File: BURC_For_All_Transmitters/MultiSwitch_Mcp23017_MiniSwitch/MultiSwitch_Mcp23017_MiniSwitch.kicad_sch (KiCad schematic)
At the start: 27 parts, among them J1 MPC23017_MODULE, J2 I2C_INPUT, J3 I2C_INPUT, J4 I2C_INPUT, J5 I2C_INPUT, J6 PCF8574, J7 PCF8574, J8 PCF8575, SW1 SW_SPST, SW10 SW_SPST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

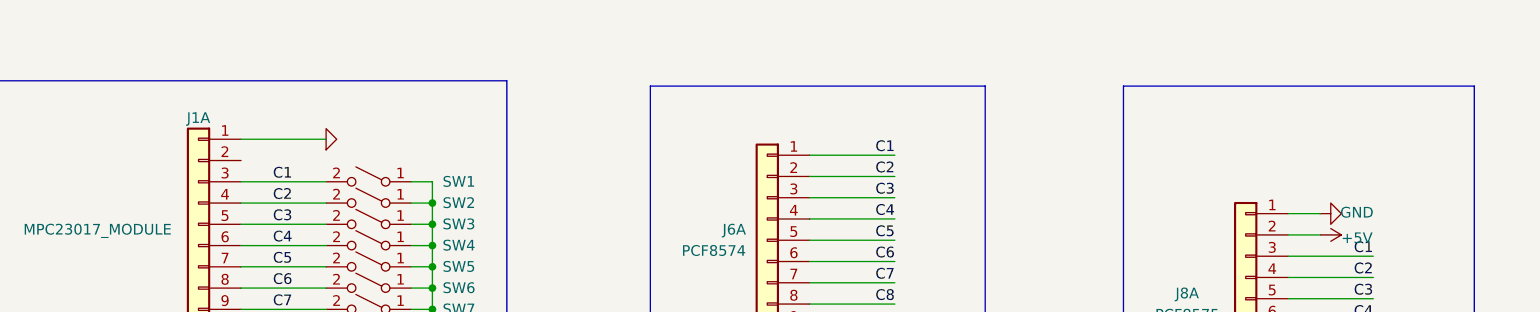
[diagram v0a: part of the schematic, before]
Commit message: Update schematic switch board
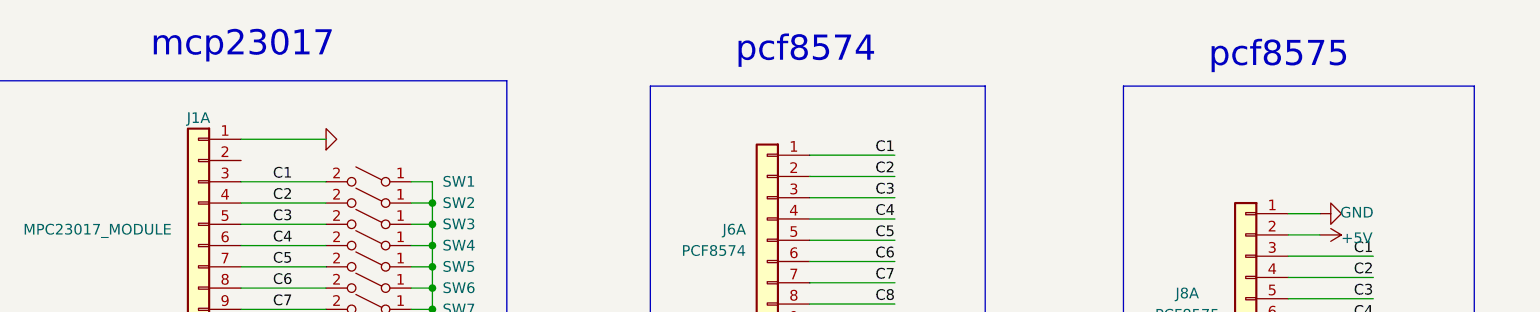
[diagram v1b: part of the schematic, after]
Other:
- note added: "mcp23017"
- note added: "pcf8574"
- note added: "pcf8575"
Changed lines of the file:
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@@
   (title_block
     (title "Board for 16 Switch")
-    (date "2023-09-02")
+    (date "2023-09-17")
     (rev "1.0")
     (company "OpenAVRc")
@@
     (stroke (width 0) (type default))
   )
+  (text "pcf8575" (at 178.435 47.625 0)
+    (effects (font (size 3 3)) (justify left bottom))
+  )
+  (text "pcf8574" (at 121.92 46.99 0)
+    (effects (font (size 3 3)) (justify left bottom))
+  )
+  (text "mcp23017" (at 52.07 46.355 0)
+    (effects (font (size 3 3)) (justify left bottom))
+  )
   (label "C2" (at 140.97 60.325 180) (fields_autoplaced)
